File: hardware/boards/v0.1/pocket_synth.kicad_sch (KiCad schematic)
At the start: 6 parts

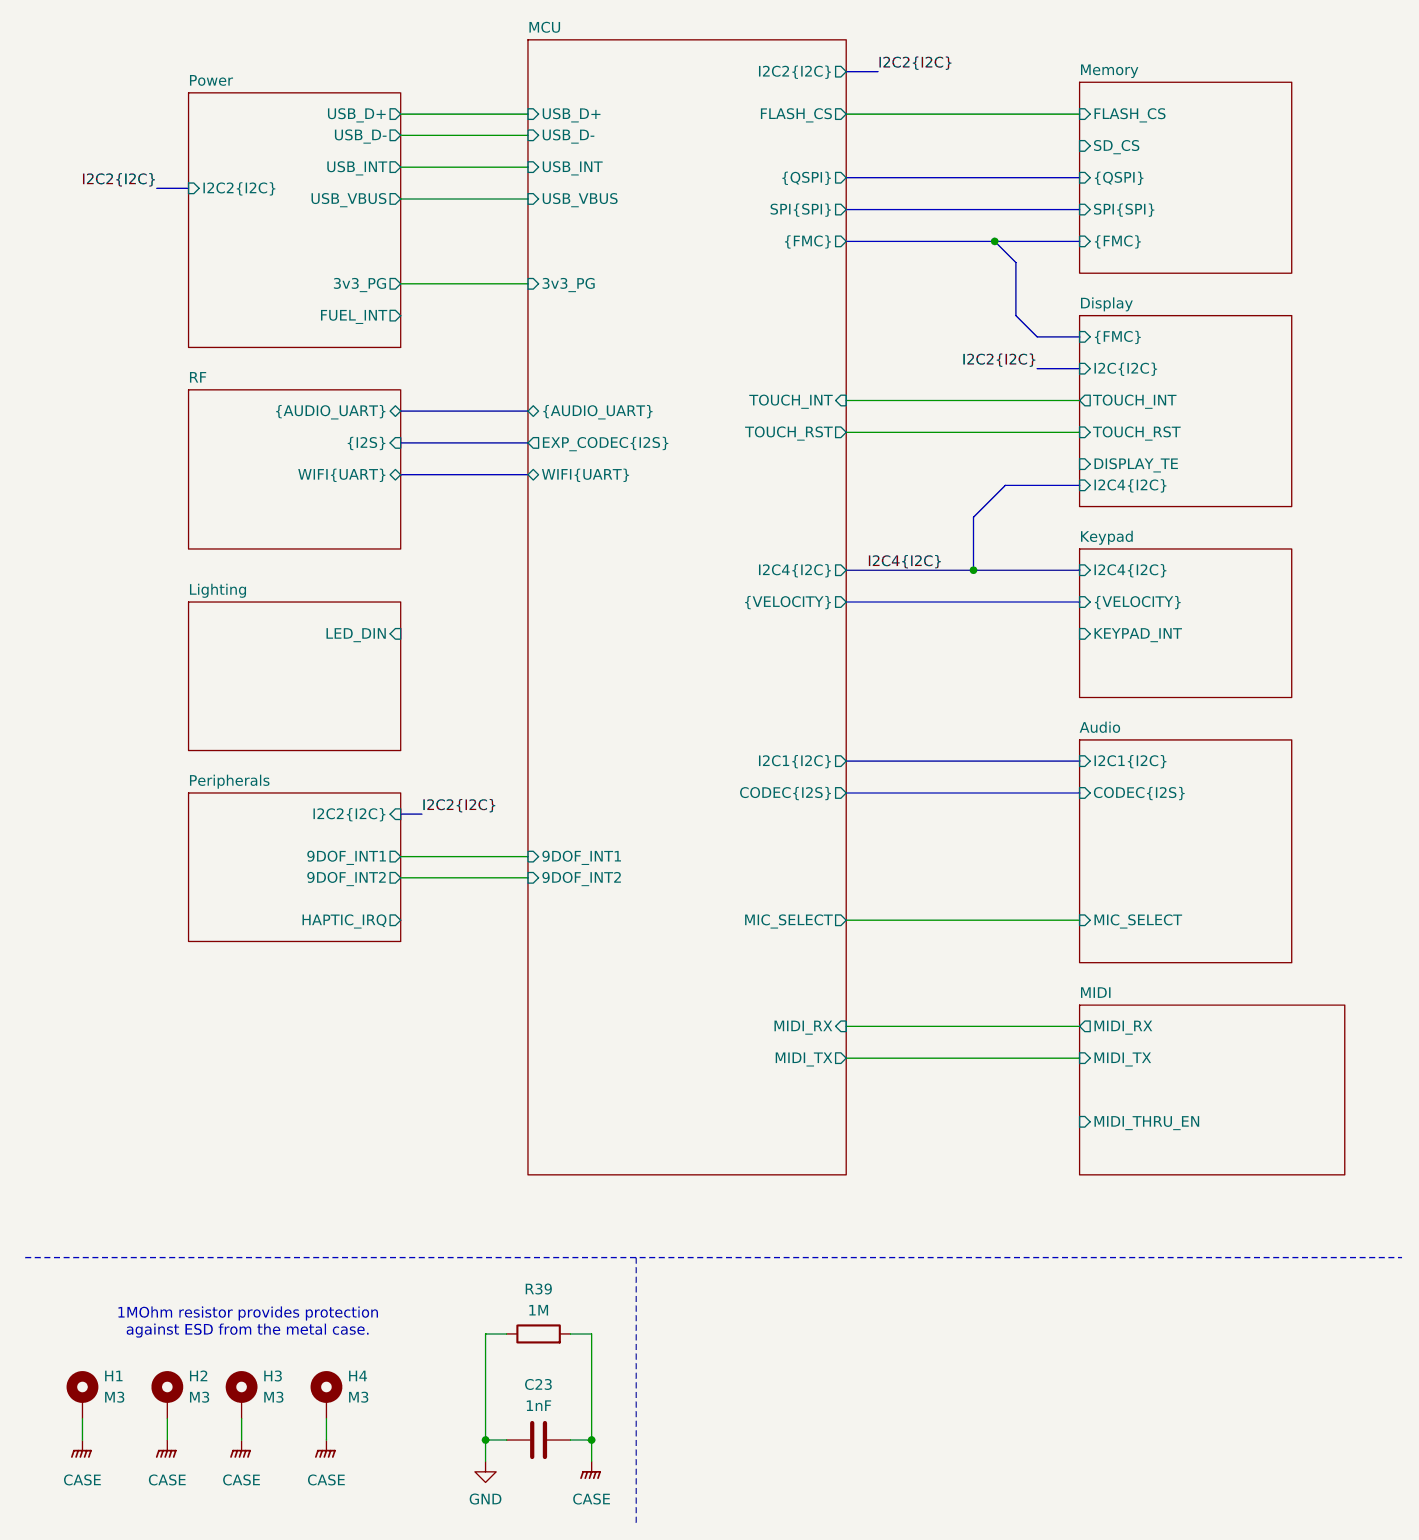
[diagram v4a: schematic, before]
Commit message: feat: various ERC and DRC cleanup
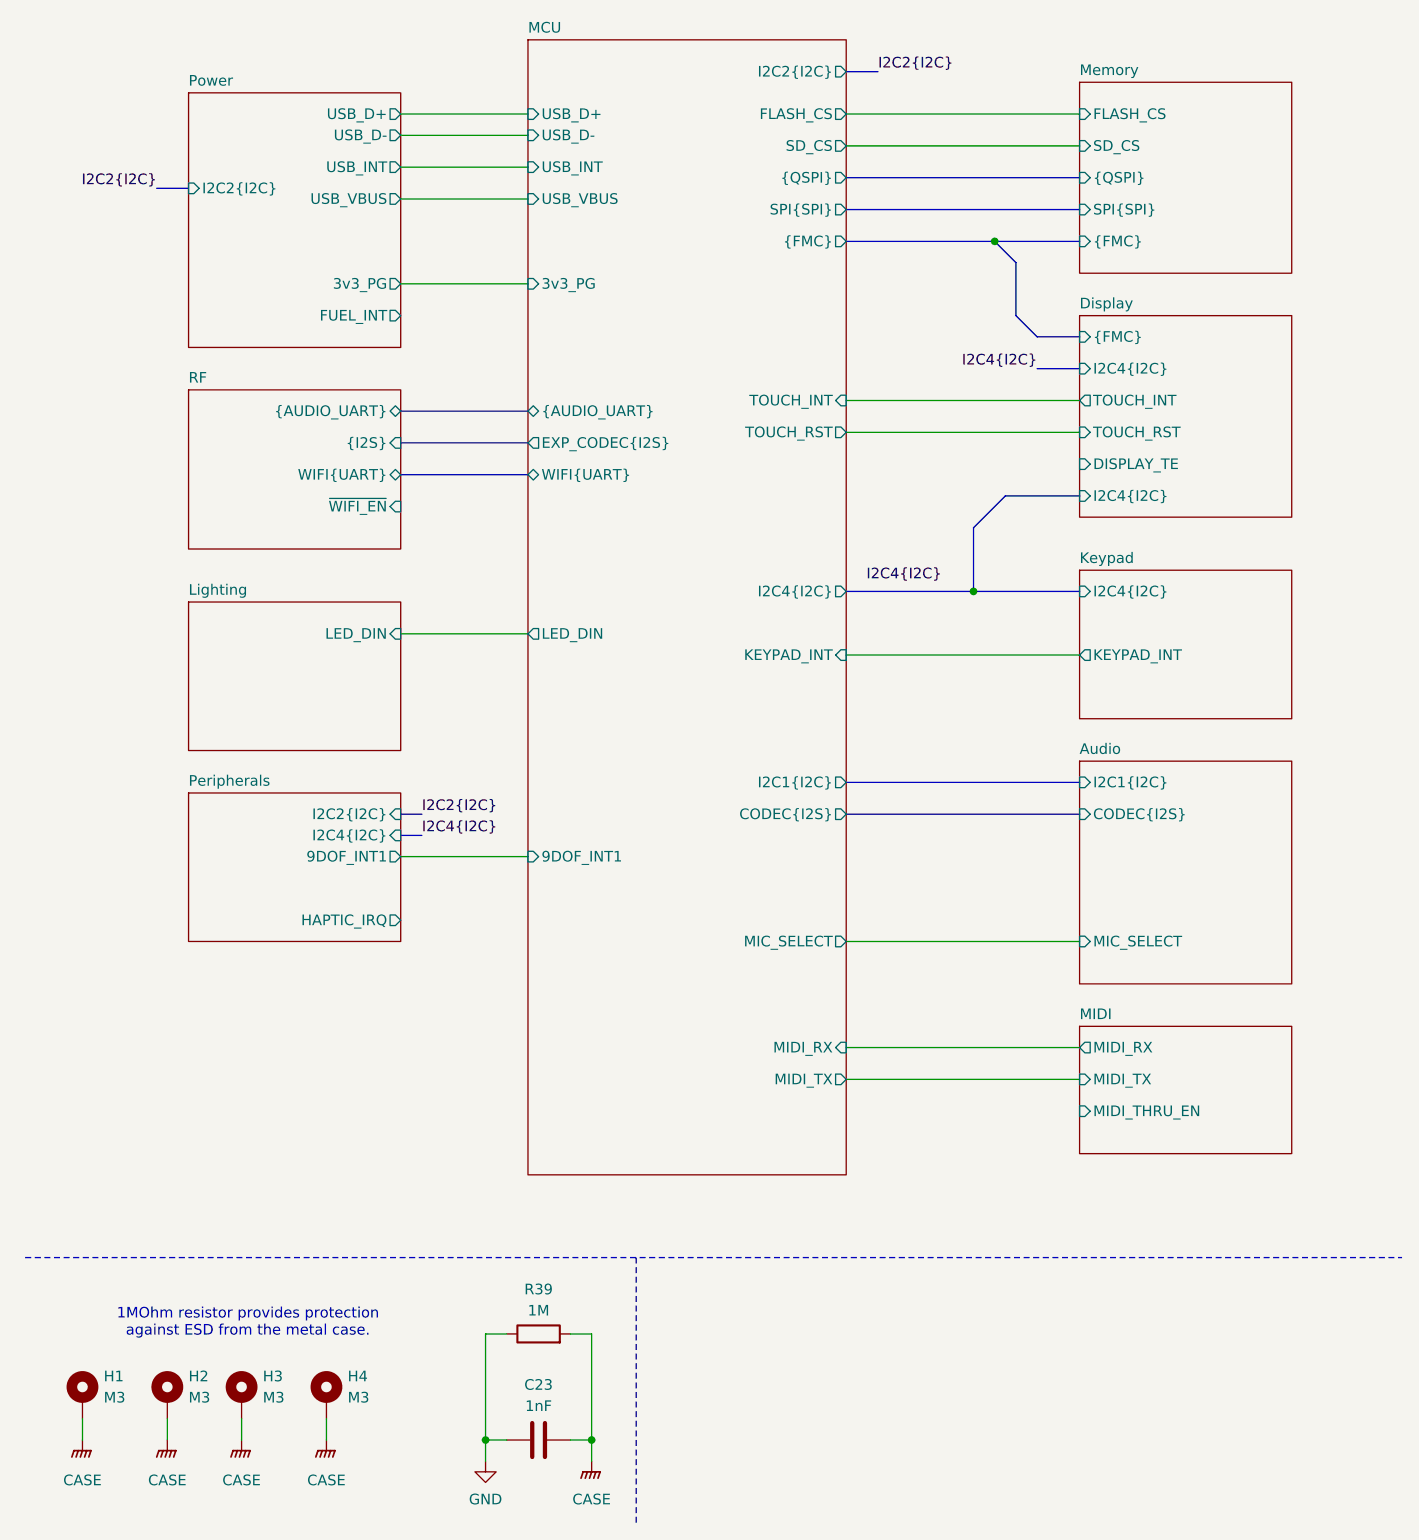
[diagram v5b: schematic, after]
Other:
- sheet Display ports: added none; removed I2C{I2C}
- sheet Keypad ports: added none; removed {VELOCITY}
- sheet MCU ports: added KEYPAD_INT, LED_DIN, SD_CS; removed 9DOF_INT2, {VELOCITY}
- sheet Peripherals ports: added I2C4{I2C}; removed 9DOF_INT2
- sheet RF ports: added ~{WIFI_EN}; removed none

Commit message: fix: more ERC cleanup
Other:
- sheet MIDI ports: added ~{MIDI_THRU_EN}; removed MIDI_THRU_EN
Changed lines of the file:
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@@
 			)
 		)
-		(pin "MIDI_THRU_EN" input
-			(at 138.43 148.59 180)
+		(pin "MIDI_TX" input
+			(at 138.43 144.78 180)
 			(effects
 				(font
@@
 			)
 		)
-		(pin "MIDI_TX" input
-			(at 138.43 144.78 180)
+		(pin "~{MIDI_THRU_EN}" input
+			(at 138.43 151.13 180)
 			(effects
 				(font

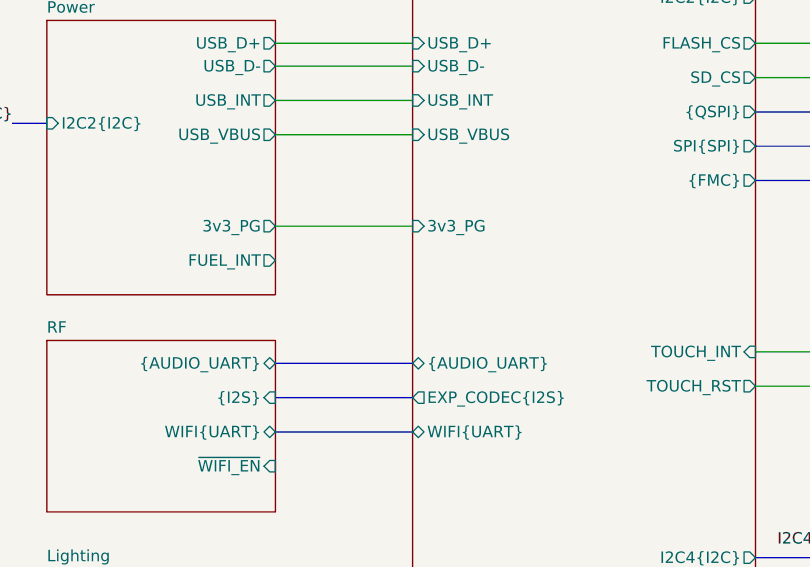
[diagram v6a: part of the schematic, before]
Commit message: feat: remove analog MIDI thru
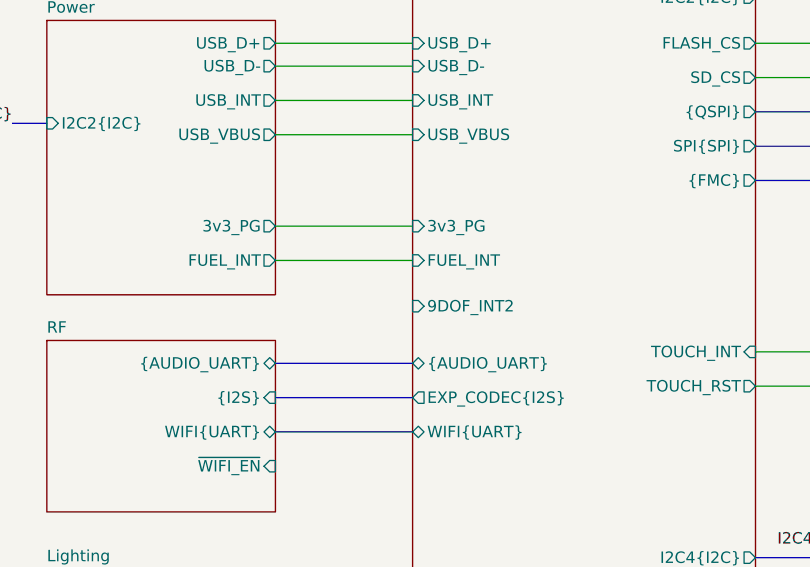
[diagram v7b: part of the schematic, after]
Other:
- sheet MCU ports: added 9DOF_INT2, FUEL_INT; removed none
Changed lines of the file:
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@@
+	(wire
+		(pts
+			(xy 57.15 53.34) (xy 72.39 53.34)
+		)
+		(stroke
+			(width 0)
+			(type default)
+		)
+	)
 	(wire
 		(pts
@@
 			(effects
 				(font
+					(size 1.27 1.27)
+				)
+				(justify left)
+			)
+		)
+		(pin "9DOF_INT2" input
+			(at 72.39 58.42 180)
+			(effects
+				(font
+					(size 1.27 1.27)
+				)
+				(justify left)
+			)
+		)
+		(pin "FUEL_INT" input
+			(at 72.39 53.34 180)
+			(effects
+				(font

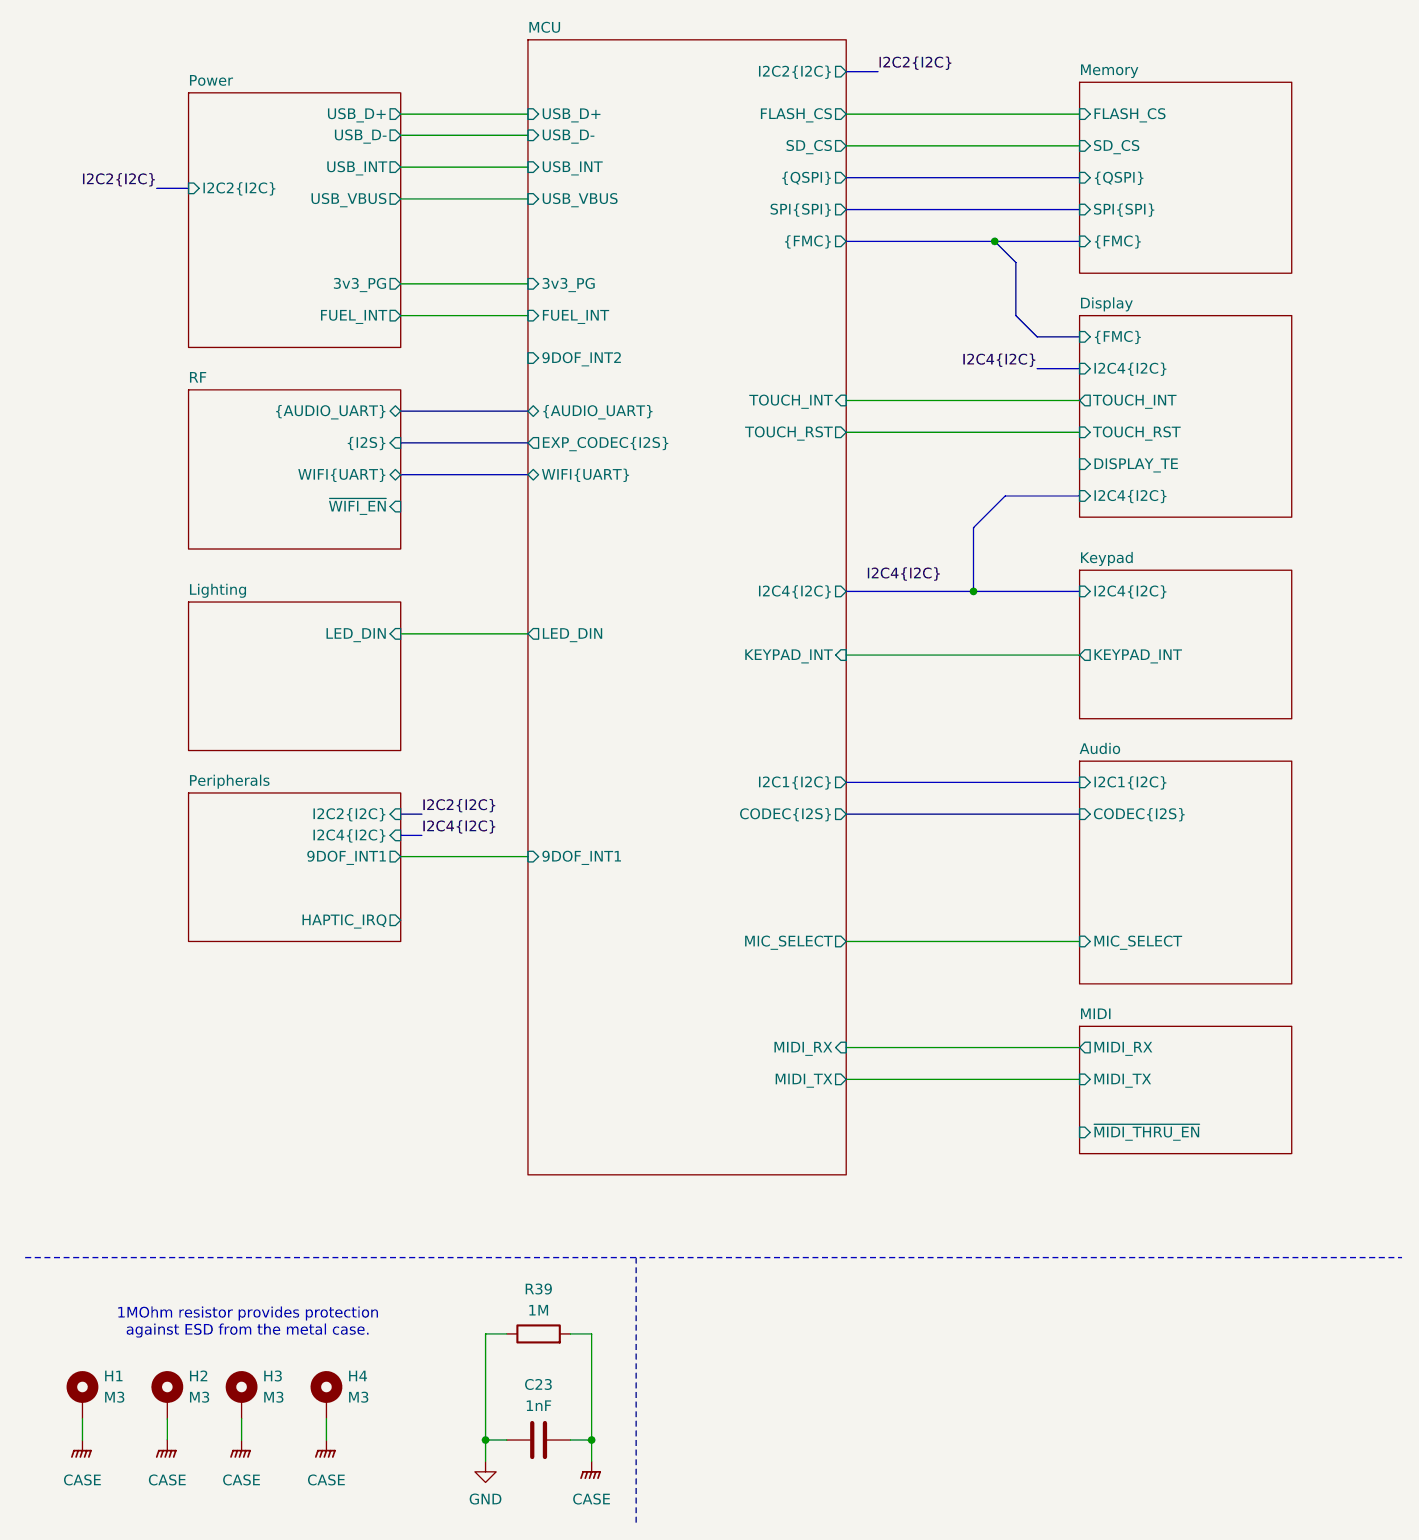
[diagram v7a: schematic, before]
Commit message: feat: more routing and DRC cleanup
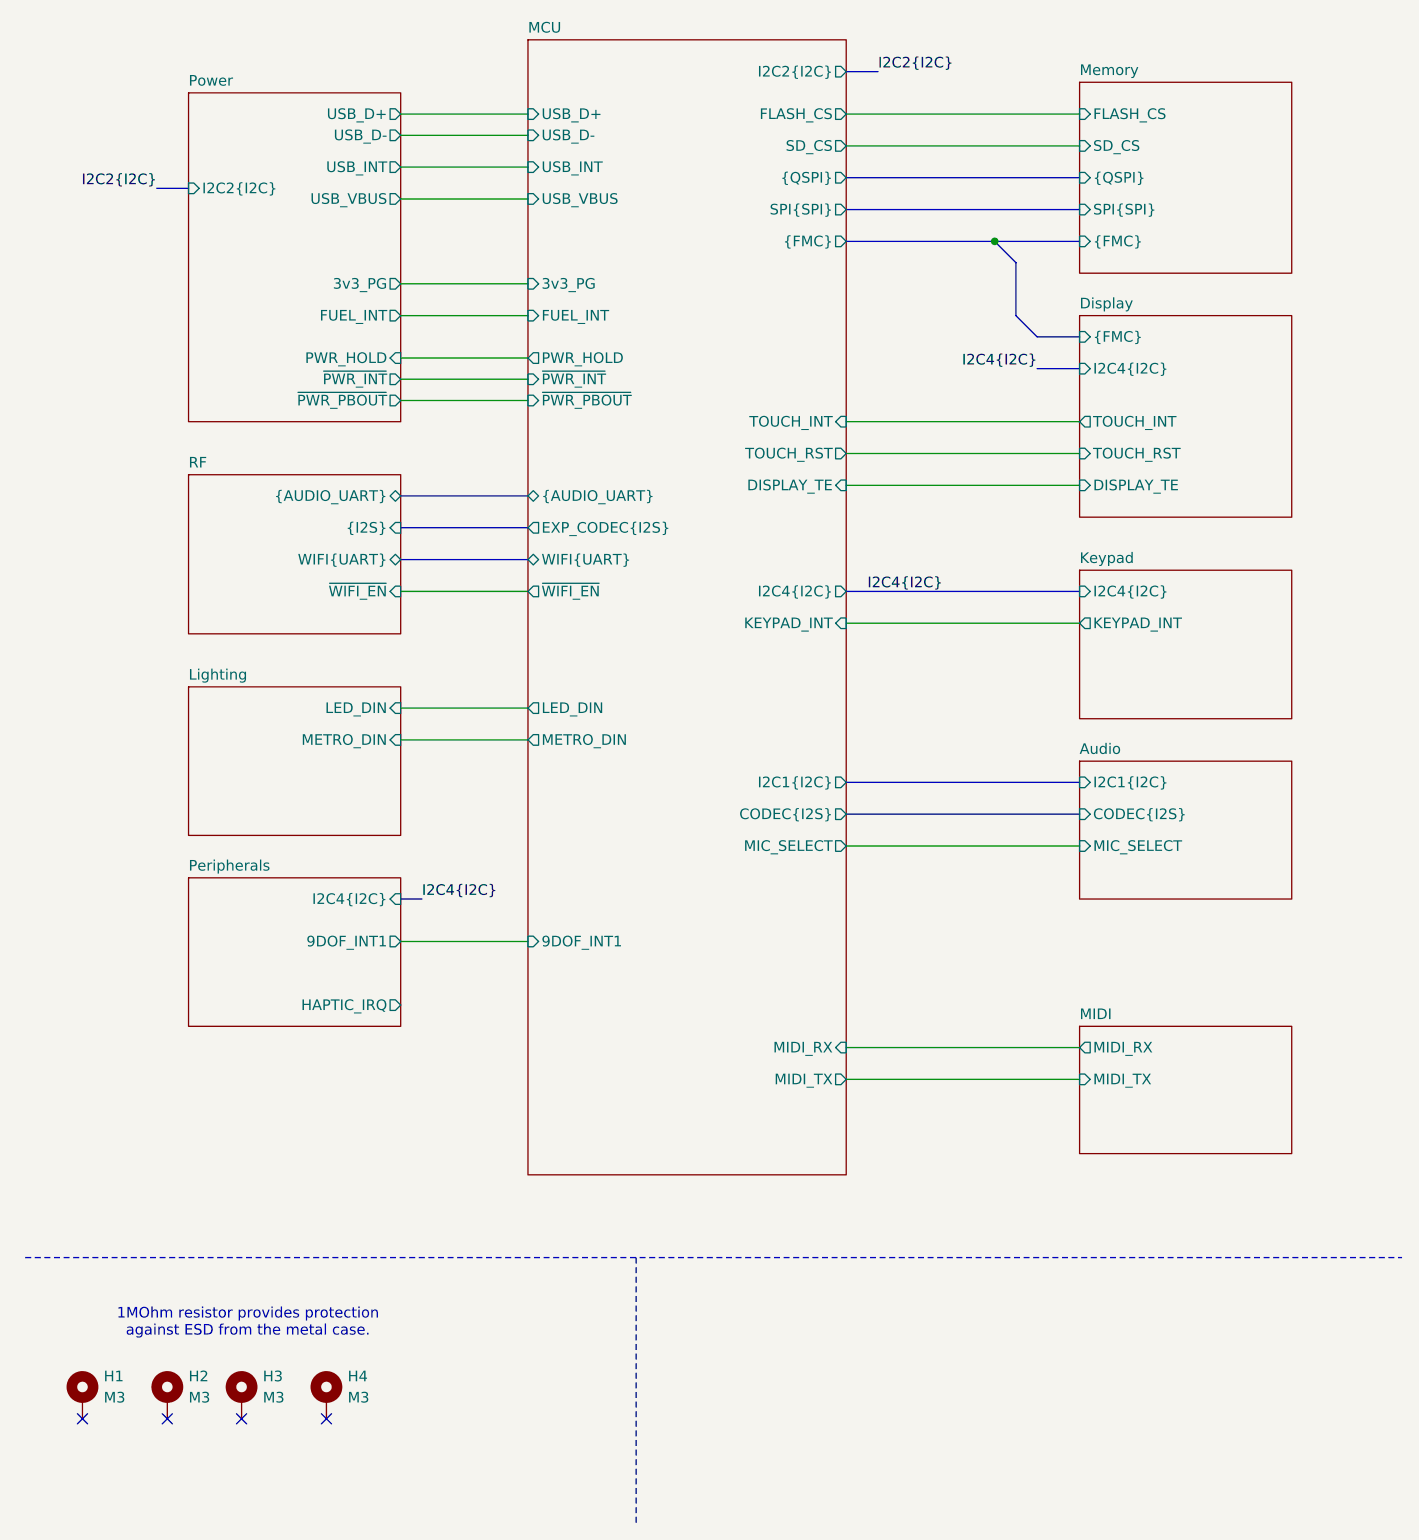
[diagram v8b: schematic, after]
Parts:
- removed C23: 1nF, symbol Device:C
- removed R39: 1M, symbol Device:R
- H1, H2, H3, H4: footprint MountingHole:MountingHole_2.2mm_M2_Pad_Via -> MountingHole:MountingHole_2.2mm_M2_Pad
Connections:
- removed net CASE: H1.1, H2.1, H3.1, H4.1
- no-connect marks 0 -> 4
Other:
- sheet Lighting ports: added METRO_DIN; removed none
- sheet MCU ports: added DISPLAY_TE, METRO_DIN, PWR_HOLD, ~{PWR_INT}, ~{PWR_PBOUT}, ~{WIFI_EN}; removed 9DOF_INT2
- sheet MIDI ports: added none; removed ~{MIDI_THRU_EN}
- sheet Peripherals ports: added none; removed I2C2{I2C}
- sheet Power ports: added PWR_HOLD, ~{PWR_INT}, ~{PWR_PBOUT}; removed none
